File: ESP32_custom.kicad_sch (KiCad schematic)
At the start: 0 parts

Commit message: process creating schematic esp32devboard
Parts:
- added C1, C2, C3, C4, C5, C6: C, symbol Device:C
- added J1: TYPE-C-31-M-12, TYPE-C-31-M-12:HRO_TYPE-C-31-M-12, symbol TYPE-C-31-M-12:TYPE-C-31-M-12
- added J2, J3: Conn_01x19_Pin, symbol Connector:Conn_01x19_Pin
- added Q1, Q2: SS8050, Package_TO_SOT_SMD:SOT-23-3, symbol Transistor_BJT:SS8050
- added R1, R2, R3, R4: R, symbol Device:R
- added SW1, SW2: SW_Push, symbol Switch:SW_Push
- added TH1, TH2, TH3, TH4, TH5, TH6: Thermistor, symbol Device:Thermistor
- added U1: ESP32-WROOM-32E 8MB, symbol 2026-08-21_16-20-42:ESP32-WROOM-32E_8MB
- added U3: CH340C, Package_SO:SOIC-16_3.9x9.9mm_P1.27mm, symbol Interface_USB:CH340C
- added U4: AMS1117-3.3, Package_TO_SOT_SMD:SOT-223-3_TabPin2, symbol Regulator_Linear:AMS1117-3.3
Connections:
- new net: C1.1, U3.13 (~{DTR})
- new net: R2.1, U3.2 (TXD)
- new net: R1.1, U3.3 (RXD)
- new net: C2.1, U3.4 (V3)
- new net: TH6.1, U1.24 (IO2)
- new net: C6.1, R4.2, SW2.1
- new net: Q1.1 (B), TH3.1
- new net: C5.1, R3.2, SW1.1
- new net: J1.S1 (SHIELD), J1.S2 (SHIELD), J1.S3 (SHIELD), J1.S4 (SHIELD)
- new net: Q2.1 (B), TH4.1
- new net: TH5.1, U1.25 (IO0)
- new net +5V: C3.1, TH1.2, TH5.2, U1.2 (3V3), U4.2 (VO)
- new net D11: J1.A7 (DN1), J1.B7 (DN2), U3.6 (UD-)
- new net D22: J1.A6 (DP1), J1.B6 (DP2), U3.5 (UD+)
- new net DRT: Q2.3 (C), TH3.2
- new net DTR: C1.2
- new net EN: Q1.3 (C), R4.1, TH1.1
- new net GND: C2.2, C3.2, C4.1, C5.2, C6.2, J1.A1_B12 (GND), J1.B1_A12 (GND), SW1.2, SW2.2, TH2.2, TH6.2, U1.1 (GND), U1.38 (GND), U1.39 (GND), U1.40 (GND), U1.41 (GND), U1.42 (GND), U1.43 (GND), U1.44 (GND), U1.45 (GND), U1.46 (GND), U1.47 (GND), U3.1 (GND), U4.1 (GND)
- new net IO0: Q2.2 (E), R3.1
- new net IO15: TH2.1
- new net RTS: Q1.2 (E), TH4.2, U3.14 (~{RTS})
- new net RX: R1.2
- new net TX: R2.2
- new net VBUS: C4.2, J1.A4_B9 (VBUS), J1.B4_A9 (VBUS), U3.16 (VCC), U4.3 (VI)

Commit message: completed schematic (v1.0)
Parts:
- removed J2, J3: Conn_01x19_Pin, symbol Connector:Conn_01x19_Pin
- added J2, J3: Conn_01x16_Pin, symbol Connector:Conn_01x16_Pin
- C1, C2, C3, C4, C5, C6: value C -> 100nF
- R: renamed from R1; value R -> 1K
- R2: value R -> 1K
- R3, R4: value R -> 470
- TH1, TH2, TH3, TH4, TH5, TH6: value Thermistor -> 10K
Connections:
- net +5V: now also J2.1 (Pin_1), J2.16 (Pin_16)
- net EN: now also U1.3 (EN), J2.2 (Pin_2)
- net GND: now also U1.15 (GND), J2.14 (Pin_14), J3.1 (Pin_1), J3.7 (Pin_7)
- net IO0: now also TH5.1, U1.25 (IO0), J3.14 (Pin_14)
- net IO15: now also J3.16 (Pin_16)
- net RX: now also U1.35 (TXD0), J3.4 (Pin_4)
- net TX: now also U1.34 (RXD0), J3.5 (Pin_5)
- net IO2: now reaches TH6.1, U1.24 (IO2)
- net IO2: now also J3.15 (Pin_15)
- net IO25: now reaches U1.10 (IO25)
- net IO25: now also J2.9 (Pin_9)
- net IO26: now reaches U1.11 (IO26)
- net IO26: now also J2.10 (Pin_10)
- net IO27: now reaches U1.12 (IO27)
- net IO27: now also J2.11 (Pin_11)
- net IO14: now reaches U1.13 (IO14)
- net IO14: now also J2.12 (Pin_12)
- net IO12: now reaches U1.14 (IO12)
- net IO12: now also J2.13 (Pin_13)
- net IO13: now reaches U1.16 (IO13)
- net IO13: now also J2.15 (Pin_15)
- net IO4: now reaches U1.26 (IO4)
- net IO4: now also J3.13 (Pin_13)
- net IO16: now reaches U1.27 (IO16)
- net IO16: now also J3.12 (Pin_12)
- net IO17: now reaches U1.28 (IO17)
- net IO17: now also J3.11 (Pin_11)
- net IO5: now reaches U1.29 (IO5)
- net IO5: now also J3.10 (Pin_10)
- net IO18: now reaches U1.30 (IO18)
- net IO18: now also J3.9 (Pin_9)
- net IO19: now reaches U1.31 (IO19)
- net IO19: now also J3.8 (Pin_8)
- net IO21: now reaches U1.33 (IO21)
- net IO21: now also J3.6 (Pin_6)
- net IO22: now reaches U1.36 (IO22)
- net IO22: now also J3.3 (Pin_3)
- net IO23: now reaches U1.37 (IO23)
- net IO23: now also J3.2 (Pin_2)
- net VP: now reaches U1.4 (SENSOR_VP)
- net VP: now also J2.3 (Pin_3)
- net VN: now reaches U1.5 (SENSOR_VN)
- net VN: now also J2.4 (Pin_4)
- net IO34: now reaches U1.6 (IO34)
- net IO34: now also J2.5 (Pin_5)
- net IO35: now reaches U1.7 (IO35)
- net IO35: now also J2.6 (Pin_6)
- net IO32: now reaches U1.8 (IO32)
- net IO32: now also J2.7 (Pin_7)
- net IO33: now reaches U1.9 (IO33)
- net IO33: now also J2.8 (Pin_8)

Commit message: passed ERC
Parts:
- removed U1: ESP32-WROOM-32E 8MB, symbol 2026-08-21_16-20-42:ESP32-WROOM-32E_8MB
- added U2: ESP32-WROOM-32E 8MB, symbol 2026-08-21_16-20-42:ESP32-WROOM-32E_8MB
- renumbered R to R1
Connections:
- net +5V: now also U2.2 (3V3)
- net EN: now also U2.3 (EN)
- net GND: now also U2.1 (GND), U2.15 (GND), U2.38 (GND), U2.39 (GND), U2.40 (GND), U2.41 (GND), U2.42 (GND), U2.43 (GND), U2.44 (GND), U2.45 (GND), U2.46 (GND), U2.47 (GND)
- net IO0: now also U2.25 (IO0)
- net IO12: now also U2.14 (IO12)
- net IO13: now also U2.16 (IO13)
- net IO14: now also U2.13 (IO14)
- net IO15: now also U2.23 (IO15)
- net IO16: now also U2.27 (IO16)
- net IO17: now also U2.28 (IO17)
- net IO18: now also U2.30 (IO18)
- net IO19: now also U2.31 (IO19)
- net IO2: now also U2.24 (IO2)
- net IO21: now also U2.33 (IO21)
- net IO22: now also U2.36 (IO22)
- net IO23: now also U2.37 (IO23)
- net IO25: now also U2.10 (IO25)
- net IO26: now also U2.11 (IO26)
- net IO27: now also U2.12 (IO27)
- net IO32: now also U2.8 (IO32)
- net IO33: now also U2.9 (IO33)
- net IO34: now also U2.6 (IO34)
- net IO35: now also U2.7 (IO35)
- net IO4: now also U2.26 (IO4)
- net IO5: now also U2.29 (IO5)
- net RX: now also U2.35 (TXD0)
- net TX: now also U2.34 (RXD0)
- net VN: now also U2.5 (SENSOR_VN)
- net VP: now also U2.4 (SENSOR_VP)
- no-connect marks 0 -> 10

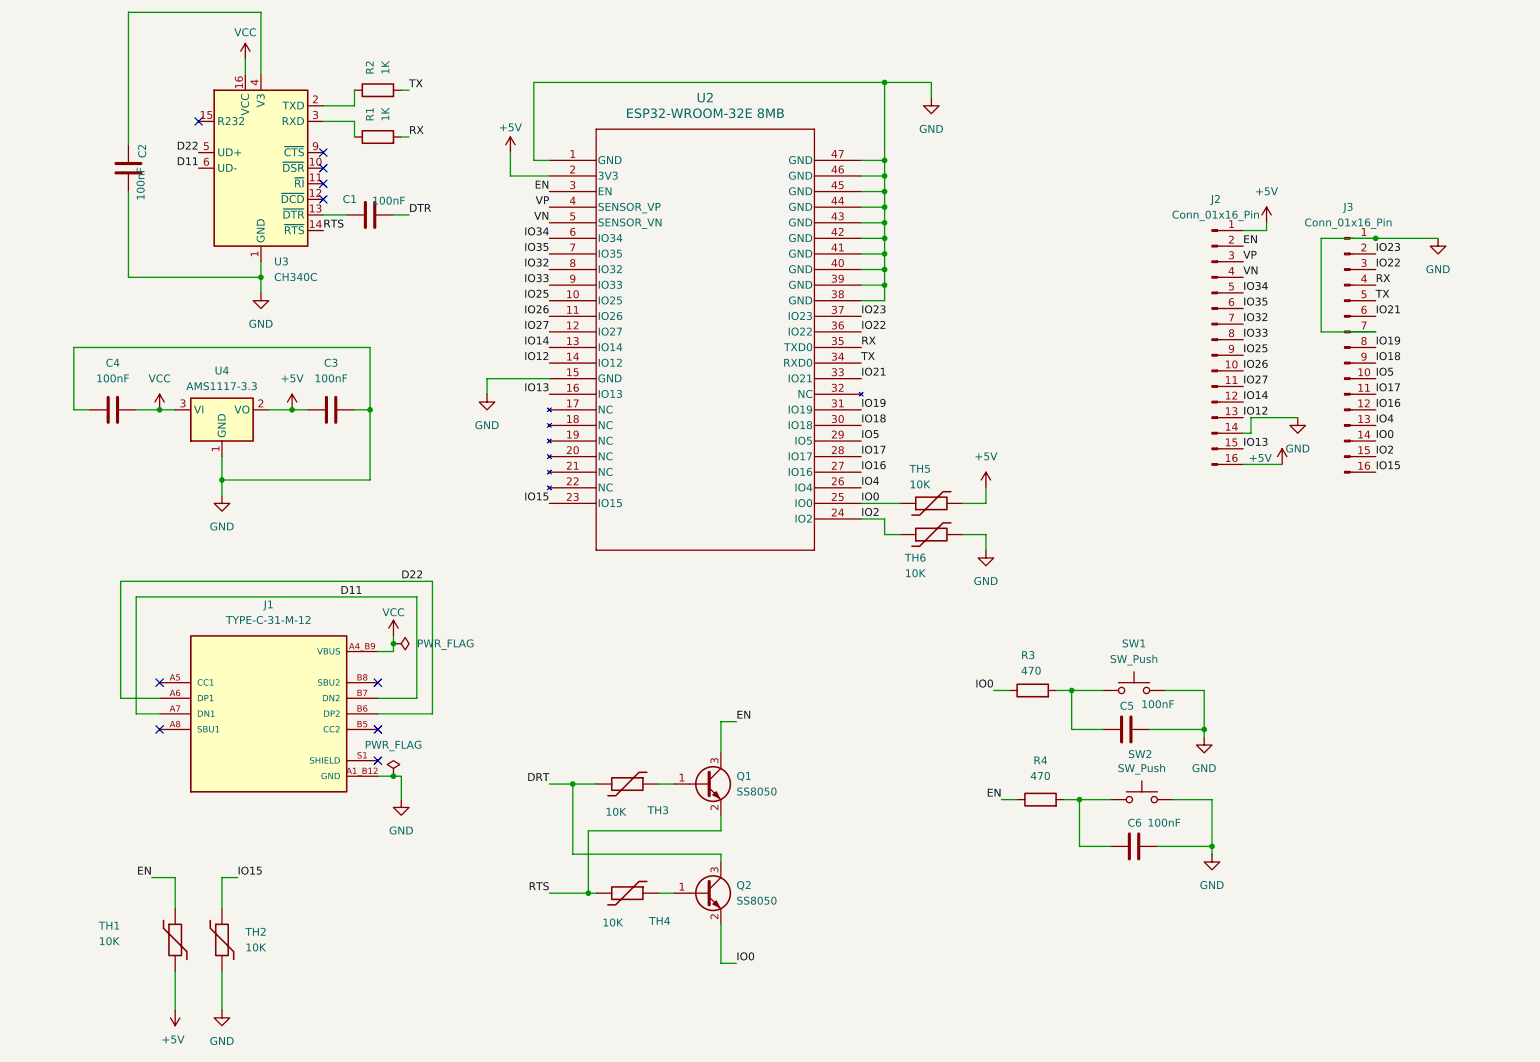
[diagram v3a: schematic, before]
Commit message: assigning footprint (undone), change component
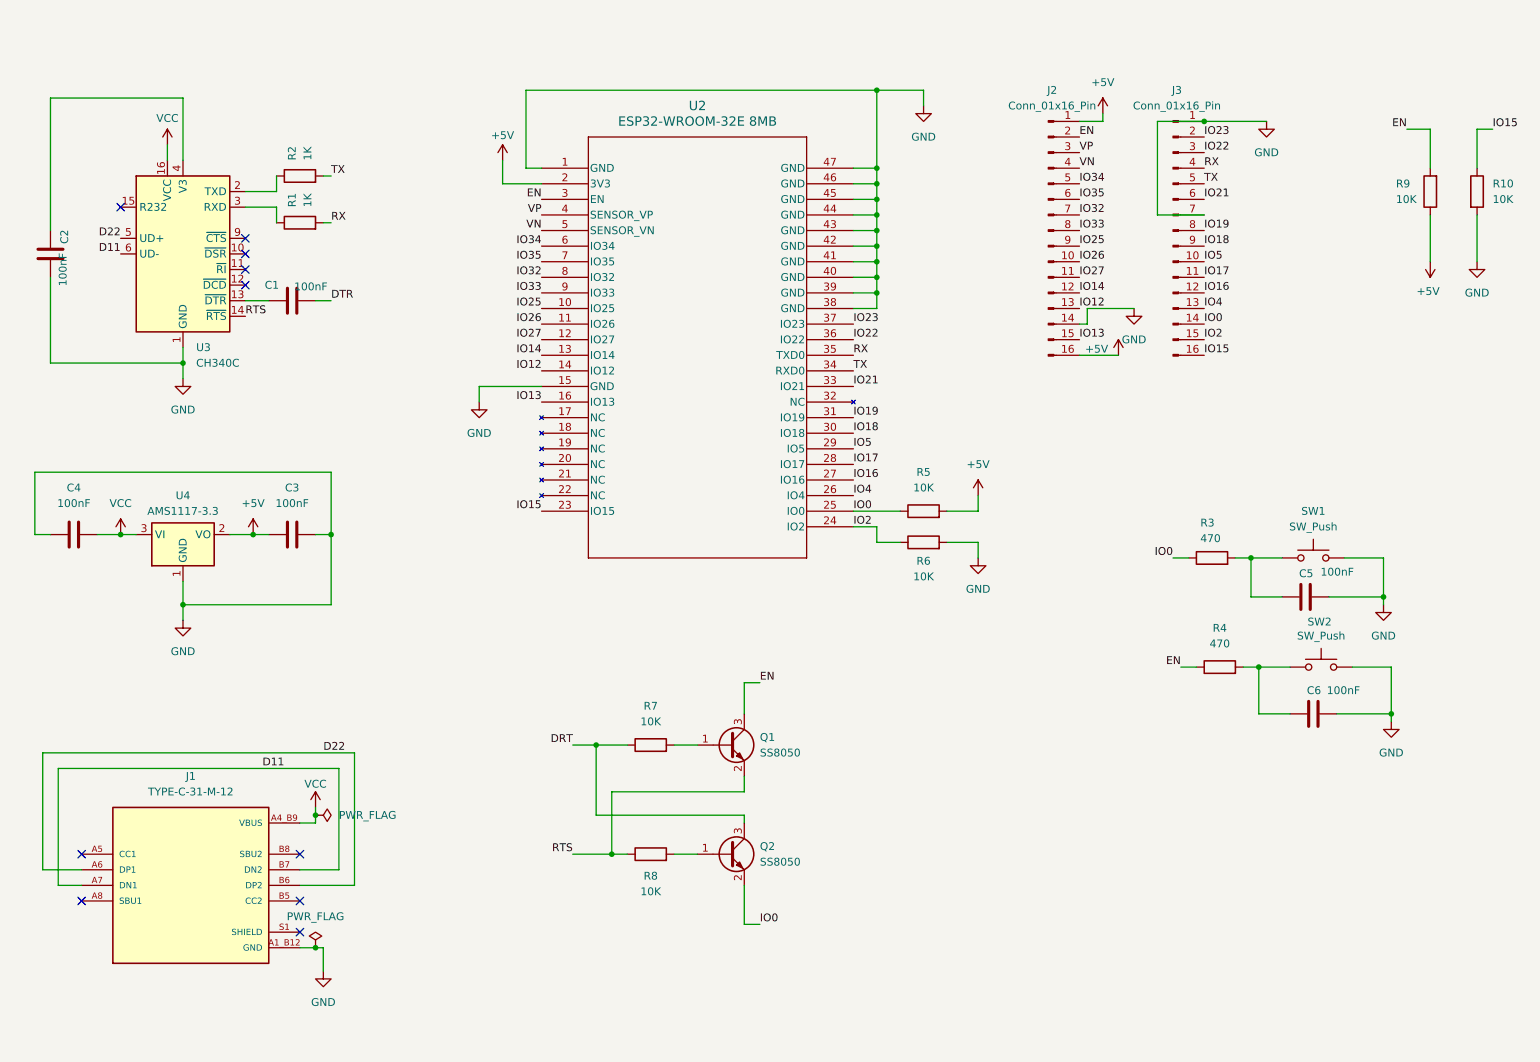
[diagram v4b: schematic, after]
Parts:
- removed TH1, TH2, TH3, TH4, TH5, TH6: 10K, symbol Device:Thermistor
- added R10, R5, R6, R7, R8, R9: 10K, symbol Device:R
- C1, C2, C3, C4, C5, C6: footprint (none) -> Capacitor_SMD:C_0402_1005Metric
- J2, J3: footprint (none) -> Connector_PinHeader_2.00mm:PinHeader_1x16_P2.00mm_Vertical
- R1, R2, R3, R4: footprint (none) -> Resistor_SMD:R_0402_1005Metric
- SW1: footprint (none) -> Button_Switch_SMD:SW_SPST_Omron_B3FS-100xP
- SW2: footprint (none) -> Button_Switch_SMD:SW_SPST_GT-TC155X
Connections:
- net +5V: now also R5.2, R9.1
- net DRT: now also R7.1
- net EN: now also R9.2
- net GND: now also R10.2, R6.2
- net IO0: now also R5.1
- net IO15: now also R10.1
- net IO2: now also R6.1
- net RTS: now also R8.1
- net at Q1.1 (B): now also R7.2
- net at Q2.1 (B): now also R8.2
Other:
- moved on the sheet: C1, C2, C3, C4, C5, C6, J1, J2, J3, Q1, Q2, R1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

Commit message: completed assign footprint
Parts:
- R10, R5, R6, R7, R8, R9: footprint (none) -> Resistor_SMD:R_0402_1005Metric
- U2: footprint (none) -> KiCADv6:ESP32­WROOM­32E_EXP
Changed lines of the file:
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@@
 			)
 		)
-		(property "Footprint" ""
+		(property "Footprint" "Resistor_SMD:R_0402_1005Metric"
 			(at 261.112 50.8 90)
 			(hide yes)
@@
 			)
 		)
-		(property "Footprint" ""
+		(property "Footprint" "Resistor_SMD:R_0402_1005Metric"
 			(at 172.72 109.728 90)
 			(hide yes)
@@
 			)
 		)
-		(property "Footprint" ""
+		(property "Footprint" "Resistor_SMD:R_0402_1005Metric"
 			(at 128.27 142.748 90)
 			(hide yes)
@@
 			)
 		)
-		(property "Footprint" ""
+		(property "Footprint" "Resistor_SMD:R_0402_1005Metric"
 			(at 172.72 104.648 90)
 			(hide yes)
@@
 			)
 		)
-		(property "Footprint" ""
+		(property "Footprint" "Resistor_SMD:R_0402_1005Metric"
 			(at 128.27 160.528 90)
 			(hide yes)
@@
 			)
 		)
-		(property "Footprint" ""
+		(property "Footprint" "KiCADv6:ESP32­WROOM­32E_EXP"
 			(at 110.49 46.99 0)
 			(hide yes)
@@
 			)
 		)
-		(property "Footprint" ""
+		(property "Footprint" "Resistor_SMD:R_0402_1005Metric"
 			(at 257.048 50.8 90)
 			(hide yes)

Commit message: arranging footprint
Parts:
- J2, J3: footprint Connector_PinHeader_2.00mm:PinHeader_1x16_P2.00mm_Vertical -> Connector_PinHeader_2.54mm:PinHeader_1x16_P2.54mm_Vertical
- SW2: footprint Button_Switch_SMD:SW_SPST_GT-TC155X -> Button_Switch_SMD:SW_SPST_Omron_B3FS-100xP
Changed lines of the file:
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@@
 			)
 		)
-		(property "Footprint" "Connector_PinHeader_2.00mm:PinHeader_1x16_P2.00mm_Vertical"
+		(property "Footprint" "Connector_PinHeader_2.54mm:PinHeader_1x16_P2.54mm_Vertical"
 			(at 193.04 57.15 0)
 			(hide yes)
@@
 			)
 		)
-		(property "Footprint" "Connector_PinHeader_2.00mm:PinHeader_1x16_P2.00mm_Vertical"
+		(property "Footprint" "Connector_PinHeader_2.54mm:PinHeader_1x16_P2.54mm_Vertical"
 			(at 213.36 57.15 0)
 			(hide yes)
@@
 			)
 		)
-		(property "Footprint" "Button_Switch_SMD:SW_SPST_GT-TC155X"
+		(property "Footprint" "Button_Switch_SMD:SW_SPST_Omron_B3FS-100xP"
 			(at 237.49 123.19 0)
 			(hide yes)

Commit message: change button footprint
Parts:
- SW1, SW2: footprint Button_Switch_SMD:SW_SPST_Omron_B3FS-100xP -> Button_Switch_SMD:SW_SPST_B3U-1000P
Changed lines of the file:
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@@
 			)
 		)
-		(property "Footprint" "Button_Switch_SMD:SW_SPST_Omron_B3FS-100xP"
+		(property "Footprint" "Button_Switch_SMD:SW_SPST_B3U-1000P"
 			(at 237.49 123.19 0)
 			(hide yes)
@@
 			)
 		)
-		(property "Footprint" "Button_Switch_SMD:SW_SPST_Omron_B3FS-100xP"
+		(property "Footprint" "Button_Switch_SMD:SW_SPST_B3U-1000P"
 			(at 236.22 105.41 0)
 			(hide yes)

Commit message: fix the schematic
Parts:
- added R11, R12: 5.1K, symbol Device:R
- C3, C4, C5: value 100nF -> 10uF
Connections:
- net +5V: now also C4.2, J1.A4_B9 (VBUS), J1.B4_A9 (VBUS), U4.3 (VI); no longer C3.1, R5.2, R9.1, U2.2 (3V3), U4.2 (VO)
- net DTR: now also Q2.2 (E), R7.1
- net GND: now also R11.2, R12.2
- net IO0: now also Q2.3 (C); no longer Q2.2 (E)
- net at J1.A5 (CC1): now also R12.1
- net at J1.B5 (CC2): now also R11.1
- removed net DRT: Q2.3 (C), R7.1
- removed net VBUS: C4.2, J1.A4_B9 (VBUS), J1.B4_A9 (VBUS), U3.16 (VCC), U4.3 (VI)
- new net VCC: C3.1, R5.2, R9.1, U2.2 (3V3), U3.16 (VCC), U4.2 (VO)
- no-connect marks 10 -> 8
